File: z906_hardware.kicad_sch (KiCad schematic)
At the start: 89 parts, among them J1 USB_C_Receptacle_USB2.0_14P, J5 Ampli, J6 Console, U1 ESP32-S3-WROOM-1, U2 TPS62A02APDDC, U3 PCM5102A, U4 TPD2EUSB30, U5 TPD1E05U06DYA, U6 TPS7A4533, U7 PCM1860DBT

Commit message: correct i2s bus
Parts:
- removed C36, C38: 1nF, Capacitor_SMD:C_0603_1608Metric_Pad1.08x0.95mm_HandSolder, symbol Device:C
- removed R12, R9: 100, Resistor_SMD:R_0805_2012Metric_Pad1.20x1.40mm_HandSolder, symbol Device:R
- removed U5: TPD1E05U06DYA, Diode_SMD:D_SOD-523, symbol Power_Protection:TPD1E05U06DYA
- added D1: PESD5V0S1BL-QYL, Diode_SMD:D_SOD-882, symbol Diode:PESD5V0L1UL
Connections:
- net GND: now also D1.1 (K)
- net at U7.3 (VINL1/VIN1P): now also C35.2
- net at U7.4 (VINR1/VIN2P): now also C37.2
- net at C6.1, F1.2, FB1.1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: now also D1.2 (A)
- net ADC_DATA renamed I2S.ADC
- net BCK renamed I2S.BCK
- net DAC_DATA renamed I2S.DAC
- net LCK renamed I2S.LCK
- net MCLK renamed I2S.MCLK
- no-connect marks 27 -> 29
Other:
- moved on the sheet: C12, C13, C35, C37, C39, R10, R11, R14, R15, R22, R23, R27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

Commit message: correct usb tvs
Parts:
- removed D1: PESD5V0S1BL-QYL, Diode_SMD:D_SOD-882, symbol Diode:PESD5V0L1UL
- added D1: PESD5V0S1UB, symbol Device:D_TVS
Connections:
- net GND: now also D1.1 (A1)
- net at C6.1, F1.2, FB1.1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: now also D1.2 (A2)
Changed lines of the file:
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@@
 	)
 	(symbol
-		(lib_id "Diode:PESD5V0L1UL")
-		(at 63.5 31.75 90)
-		(unit 1)
-		(body_style 1)
-		(exclude_from_sim no)
-		(in_bom yes)
-		(on_board yes)
-		(in_pos_files yes)
-		(dnp no)
-		(fields_autoplaced yes)
-		(property "Reference" "D1"
-			(at 66.04 30.4799 90)
-			(show_name no)
-			(do_not_autoplace no)
-			(effects
-				(font
-					(size 1.27 1.27)
-				)
-				(justify right)
-			)
-		)
-		(property "Value" "PESD5V0S1BL-QYL"
-			(at 66.04 33.0199 90)
-			(show_name no)
-			(do_not_autoplace no)
-			(effects
-				(font
-					(size 1.27 1.27)
-				)
-				(justify right)
-			)
-		)
-		(property "Footprint" "Diode_SMD:D_SOD-882"
-			(at 68.58 31.75 0)
-			(hide yes)
-			(show_name no)
-			(do_not_autoplace no)
-			(effects
-				(font
-					(size 1.27 1.27)
-				)
-			)
-		)
-		(property "Datasheet" "https://assets.nexperia.com/documents/data-sheet/PESD5V0L1UL.pdf"
-			(at 58.42 31.75 0)
-			(hide yes)
-			(show_name no)
-			(do_not_autoplace no)
-			(effects
-				(font
-					(size 1.27 1.27)
-				)
-			)
-		)
-		(property "Description" "Low capacitance unidirectional ESD protection diode, 5V, SOD-882"
-			(at 55.88 31.75 0)
-			(hide yes)
-			(show_name no)
-			(do_not_autoplace no)
-			(effects
-				(font
-					(size 1.27 1.27)
-				)
-			)
-		)
-		(pin "1"
-		)
-		(pin "2"
-		)
-		(instances
-			(project "z906_hardware"
-				(path "/eb724320-f684-4550-84c5-ad44b13c3624"
-					(reference "D1")
-					(unit 1)
-				)
-			)
-		)
-	)
-	(symbol
 		(lib_id "Device:C")
 		(at 168.91 167.64 0)
@@
 					(unit 1)
 				)
+			)
+		)
+	)
+	(symbol
+		(lib_id "Device:D_TVS")
+		(at 63.5 31.75 90)
+		(unit 1)
+		(body_style 1)
+		(exclude_from_sim no)
+		(in_bom yes)
+		(on_board yes)
+		(in_pos_files yes)
+		(dnp no)
+		(fields_autoplaced yes)
+		(property "Reference" "D1"
+			(at 66.04 30.4799 90)
+			(show_name no)
+			(do_not_autoplace no)
+			(effects
+				(font
+					(size 1.27 1.27)
+				)
+				(justify right)
+			)
+		)
+		(property "Value" "PESD5V0S1UB"
+			(at 66.04 33.0199 90)
+			(show_name no)
+			(do_not_autoplace no)
+			(effects
+				(font
+					(size 1.27 1.27)
+				)
+				(justify right)
+			)
+		)
+		(property "Footprint" ""
+			(at 63.5 31.75 0)
+			(hide yes)
+			(show_name no)
+			(do_not_autoplace no)
+			(effects
+				(font
+					(size 1.27 1.27)
+				)
+			)
+		)
+		(property "Datasheet" ""
+			(at 63.5 31.75 0)
+			(hide yes)
+			(show_name no)
+			(do_not_autoplace no)
+			(effects
+				(font
+					(size 1.27 1.27)
+				)
+			)
+		)
+		(property "Description" "Bidirectional transient-voltage-suppression diode"
+			(at 63.5 31.75 0)
+			(hide yes)
+			(show_name no)
+			(do_not_autoplace no)
+			(effects
+				(font
+					(size 1.27 1.27)
+				)
+			)
+		)
+		(pin "2"
+		)
+		(pin "1"
+		)
+		(instances
+			(project "z906_hardware"
+				(path "/eb724320-f684-4550-84c5-ad44b13c3624"
+					(reference "D1")
+					(unit 1)
+				)

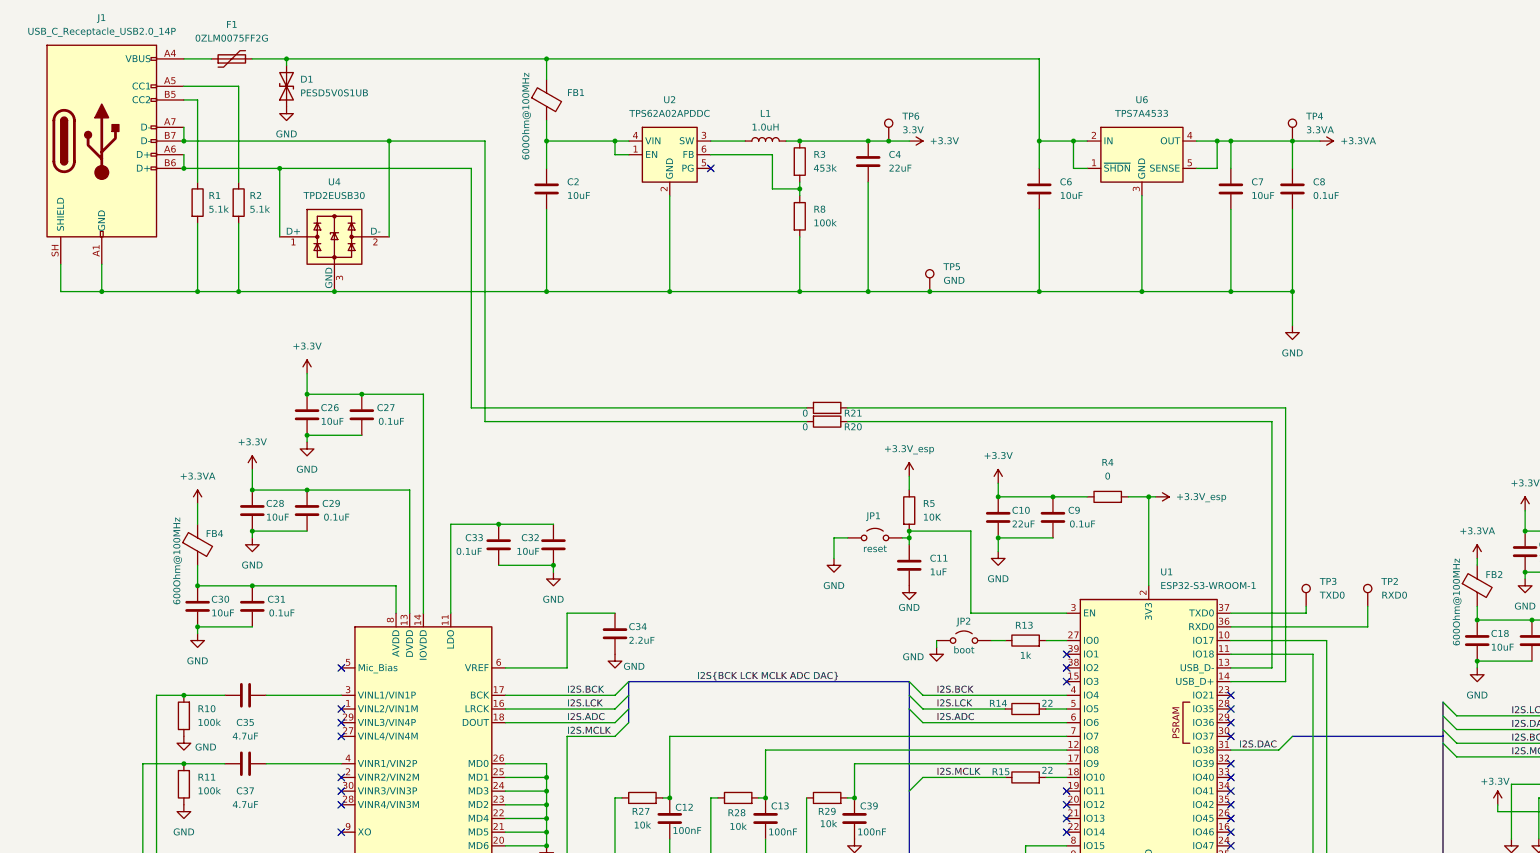
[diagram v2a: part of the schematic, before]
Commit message: change usb-c symbole for 16pin
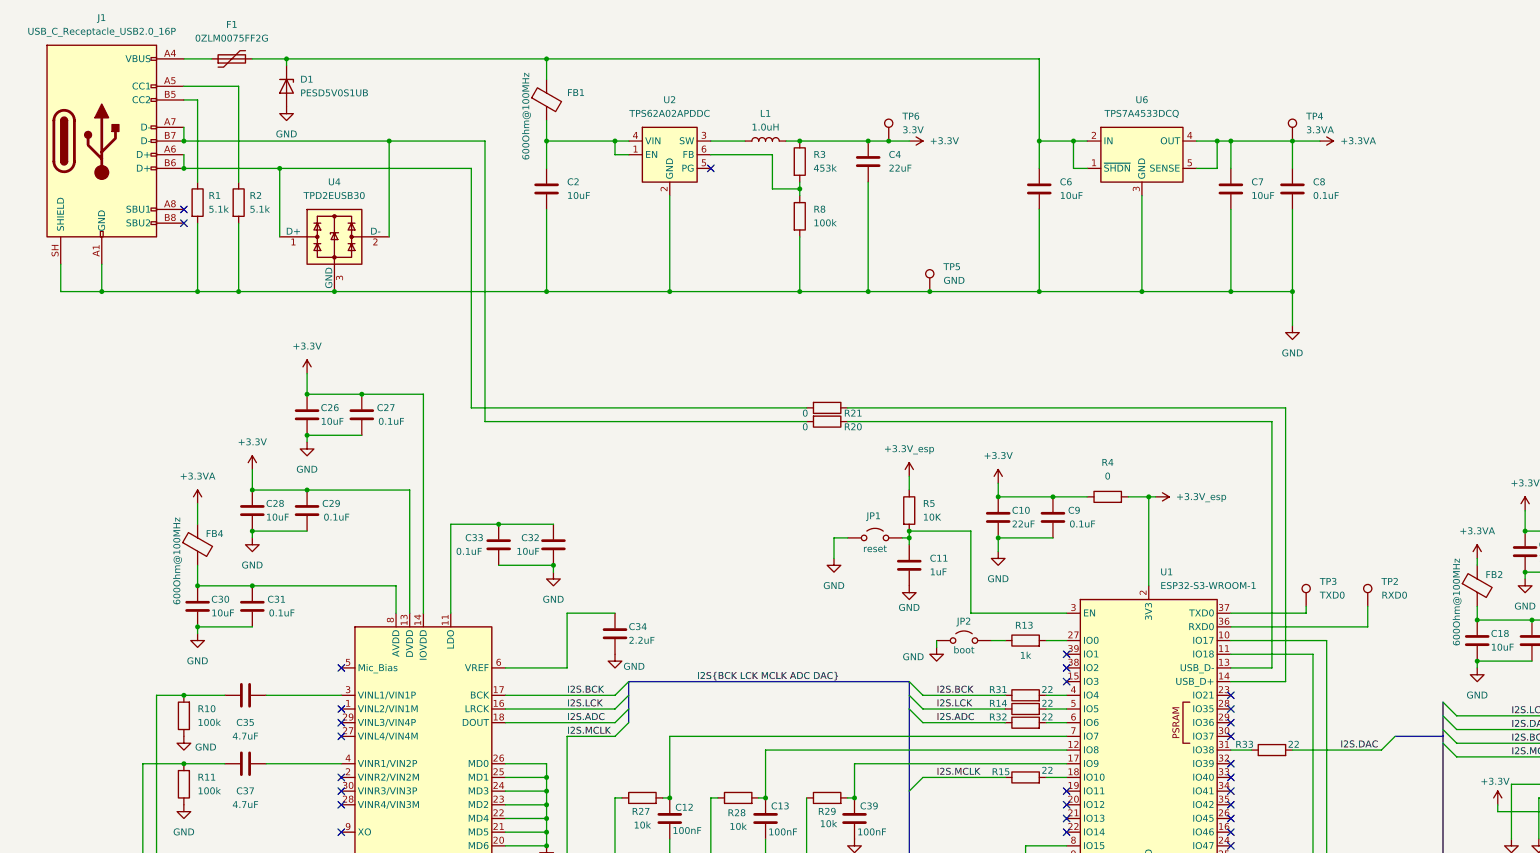
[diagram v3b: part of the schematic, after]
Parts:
- removed D1: PESD5V0S1UB, symbol Device:D_TVS
- removed J1: USB_C_Receptacle_USB2.0_14P, Connector_USB:USB_C_Receptacle_GCT_USB4105-xx-A_16P_TopMnt_Horizontal, symbol Connector:USB_C_Receptacle_USB2.0_14P
- added D1: PESD5V0S1UB, Diode_SMD:D_SOD-882, symbol Diode:PESD5V0S1UL
- added J1: USB_C_Receptacle_USB2.0_16P, symbol Connector:USB_C_Receptacle_USB2.0_16P
- added R31, R32, R33: 22, Resistor_SMD:R_0805_2012Metric_Pad1.20x1.40mm_HandSolder, symbol Device:R
- U6: value TPS7A4533 -> TPS7A4533DCQ
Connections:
- net GND: now also D1.2 (A), J1.A1 (GND), J1.A12 (GND), J1.B1 (GND), J1.B12 (GND), J1.SH (SHIELD)
- net I2S.ADC: now also R32.1; no longer U1.6 (IO6)
- net I2S.BCK: now also R31.1; no longer U1.4 (IO4)
- net I2S.DAC: now also R33.2; no longer U1.31 (IO38)
- net at R2.1: now also J1.A5 (CC1)
- net at R20.2, U4.2 (D-): now also J1.A7 (D-), J1.B7 (D-)
- net at R1.1: now also J1.B5 (CC2)
- net at F1.1: now also J1.A4 (VBUS), J1.A9 (VBUS), J1.B4 (VBUS), J1.B9 (VBUS)
- net at C6.1, F1.2, FB1.1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: now also D1.1 (K)
- net at R21.2, U4.1 (D+): now also J1.A6 (D+), J1.B6 (D+)
- new net: R31.2, U1.4 (IO4)
- new net: R33.1, U1.31 (IO38)
- new net: R32.2, U1.6 (IO6)
- no-connect marks 29 -> 31

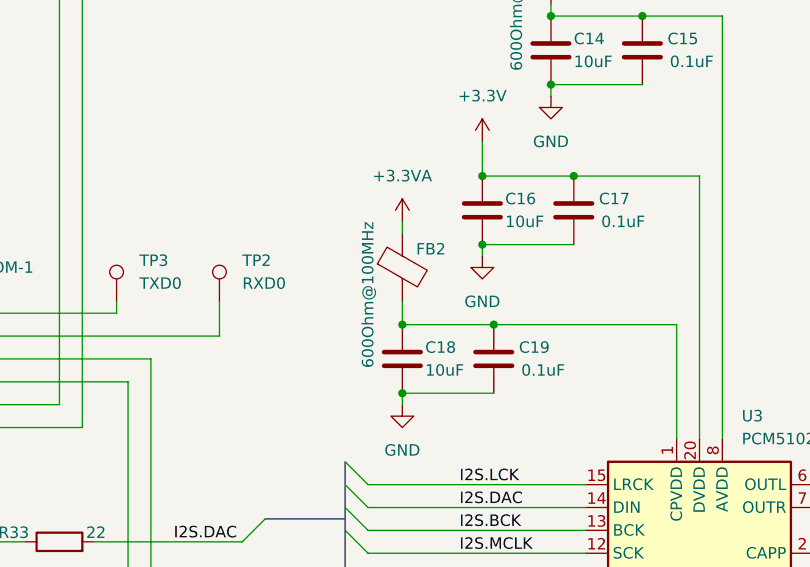
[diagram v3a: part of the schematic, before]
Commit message: remove dac fb
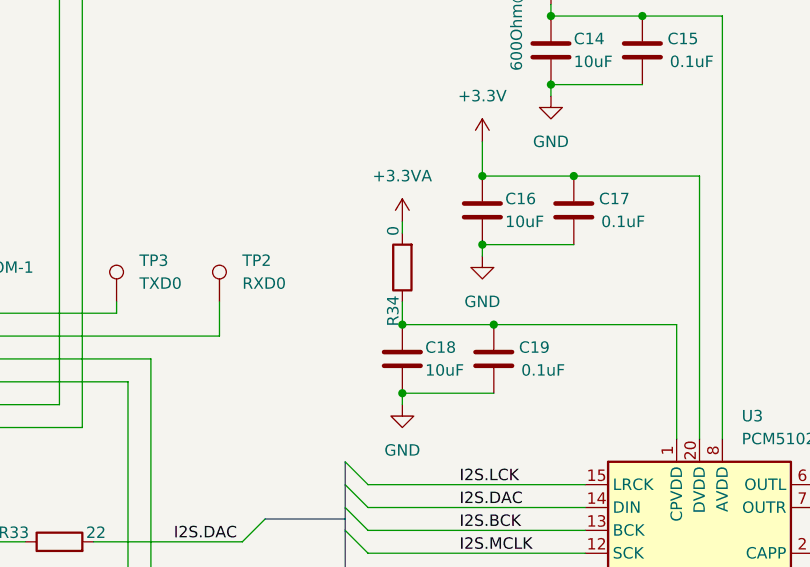
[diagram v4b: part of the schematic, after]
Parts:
- removed FB2: 600Ohm@100MHz, Resistor_SMD:R_0805_2012Metric_Pad1.20x1.40mm_HandSolder, symbol Device:FerriteBead
- added R34: 0, Resistor_SMD:R_0805_2012Metric_Pad1.20x1.40mm_HandSolder, symbol Device:R
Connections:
- net +3.3VA: now also R34.2
- net at C18.1, C19.1, U3.1 (CPVDD): now also R34.1
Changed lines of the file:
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@@
-	)
-	(symbol
-		(lib_id "Device:FerriteBead")
-		(at 284.48 124.46 0)
-		(unit 1)
-		(body_style 1)
-		(exclude_from_sim no)
-		(in_bom yes)
-		(on_board yes)
-		(in_pos_files yes)
-		(dnp no)
-		(property "Reference" "FB2"
-			(at 286.004 122.428 0)
-			(show_name no)
-			(do_not_autoplace no)
-			(effects
-				(font
-					(size 1.27 1.27)
-				)
-				(justify left)
-			)
-		)
-		(property "Value" "600Ohm@100MHz"
-			(at 280.67 135.636 90)
-			(show_name no)
-			(do_not_autoplace no)
-			(effects
-				(font
-					(size 1.27 1.27)
-				)
-				(justify left)
-			)
-		)
-		(property "Footprint" "Resistor_SMD:R_0805_2012Metric_Pad1.20x1.40mm_HandSolder"
-			(at 282.702 124.46 90)
-			(hide yes)
-			(show_name no)
-			(do_not_autoplace no)
-			(effects
-				(font
-					(size 1.27 1.27)
-				)
-			)
-		)
-		(property "Datasheet" ""
-			(at 284.48 124.46 0)
-			(hide yes)
-			(show_name no)
-			(do_not_autoplace no)
-			(effects
-				(font
-					(size 1.27 1.27)
-				)
-			)
-		)
-		(property "Description" "BLM21SP601SN1D"
-			(at 284.48 124.46 0)
-			(hide yes)
-			(show_name no)
-			(do_not_autoplace no)
-			(effects
-				(font
-					(size 1.27 1.27)
-				)
-			)
-		)
-		(pin "1"
-		)
-		(pin "2"
-		)
-		(instances
-			(project "z906_hardware"
-				(path "/eb724320-f684-4550-84c5-ad44b13c3624"
-					(reference "FB2")
-					(unit 1)
-				)
-			)
-		)
 	)
 	(symbol
@@
 					(unit 1)
 				)
+			)
+		)
+	)
+	(symbol
+		(lib_id "Device:R")
+		(at 284.48 124.46 180)
+		(unit 1)
+		(body_style 1)
+		(exclude_from_sim no)
+		(in_bom yes)
+		(on_board yes)
+		(in_pos_files yes)
+		(dnp no)
+		(property "Reference" "R34"
+			(at 283.464 129.286 90)
+			(show_name no)
+			(do_not_autoplace no)
+			(effects
+				(font
+					(size 1.27 1.27)
+				)
+			)
+		)
+		(property "Value" "0"
+			(at 283.464 120.396 90)
+			(show_name no)
+			(do_not_autoplace no)
+			(effects
+				(font
+					(size 1.27 1.27)
+				)
+			)
+		)
+		(property "Footprint" "Resistor_SMD:R_0805_2012Metric_Pad1.20x1.40mm_HandSolder"
+			(at 286.258 124.46 90)
+			(hide yes)
+			(show_name no)
+			(do_not_autoplace no)
+			(effects
+				(font
+					(size 1.27 1.27)
+				)
+			)
+		)
+		(property "Datasheet" ""
+			(at 284.48 124.46 0)
+			(hide yes)
+			(show_name no)
+			(do_not_autoplace no)
+			(effects
+				(font
+					(size 1.27 1.27)
+				)
+			)
+		)
+		(property "Description" "Resistor"
+			(at 284.48 124.46 0)
+			(hide yes)
+			(show_name no)
+			(do_not_autoplace no)
+			(effects
+				(font
+					(size 1.27 1.27)
+				)
+			)
+		)
+		(pin "1"
+		)
+		(pin "2"
+		)
+		(instances
+			(project "z906_hardware"
+				(path "/eb724320-f684-4550-84c5-ad44b13c3624"
+					(reference "R34")
+					(unit 1)
+				)

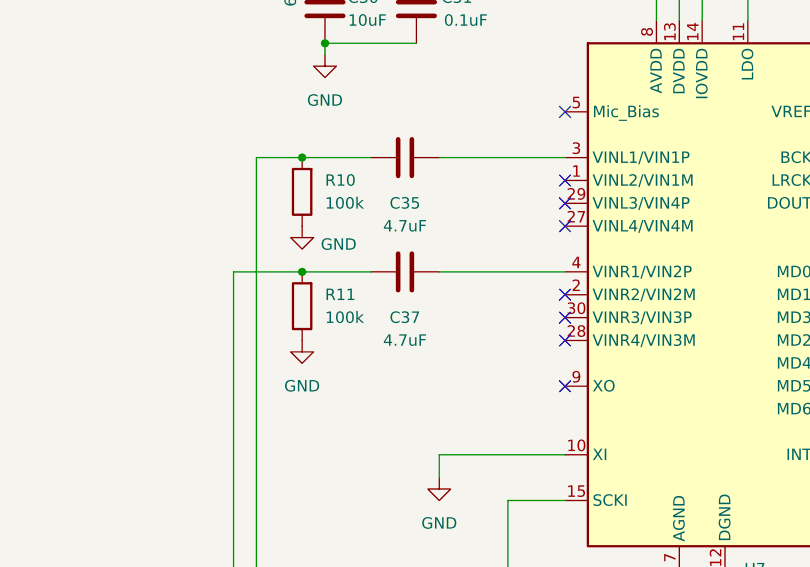
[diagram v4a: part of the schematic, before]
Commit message: use 10uF C for adc audio input
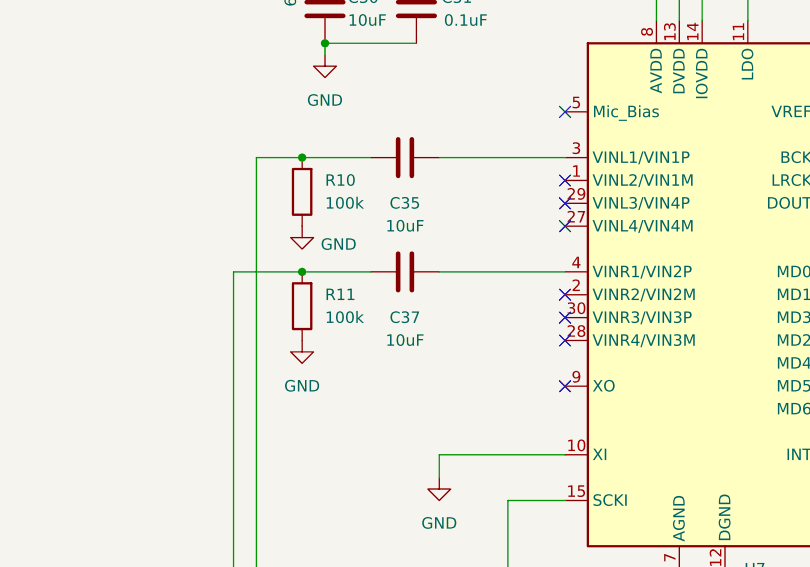
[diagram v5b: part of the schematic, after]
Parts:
- C35, C37: value 4.7uF -> 10uF
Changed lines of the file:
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@@
 			)
 		)
-		(property "Value" "4.7uF"
+		(property "Value" "10uF"
 			(at 55.88 165.1 90)
 			(show_name no)
@@
 			)
 		)
-		(property "Value" "4.7uF"
+		(property "Value" "10uF"
 			(at 55.88 152.4 90)
 			(show_name no)

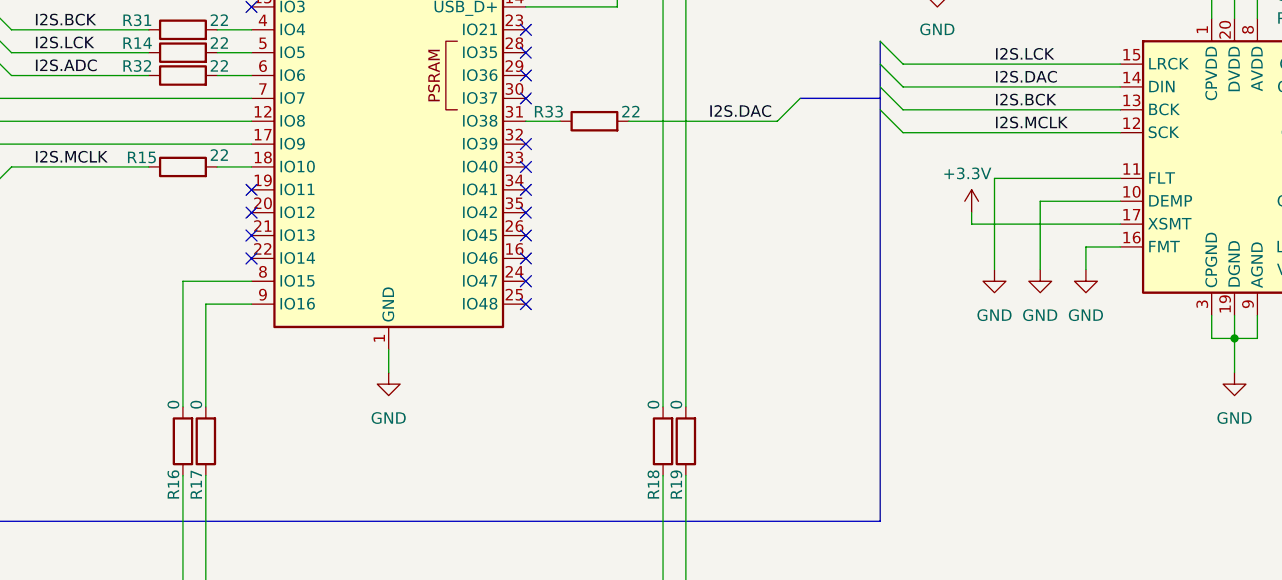
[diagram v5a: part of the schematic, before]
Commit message: use 1k ohm for uart line
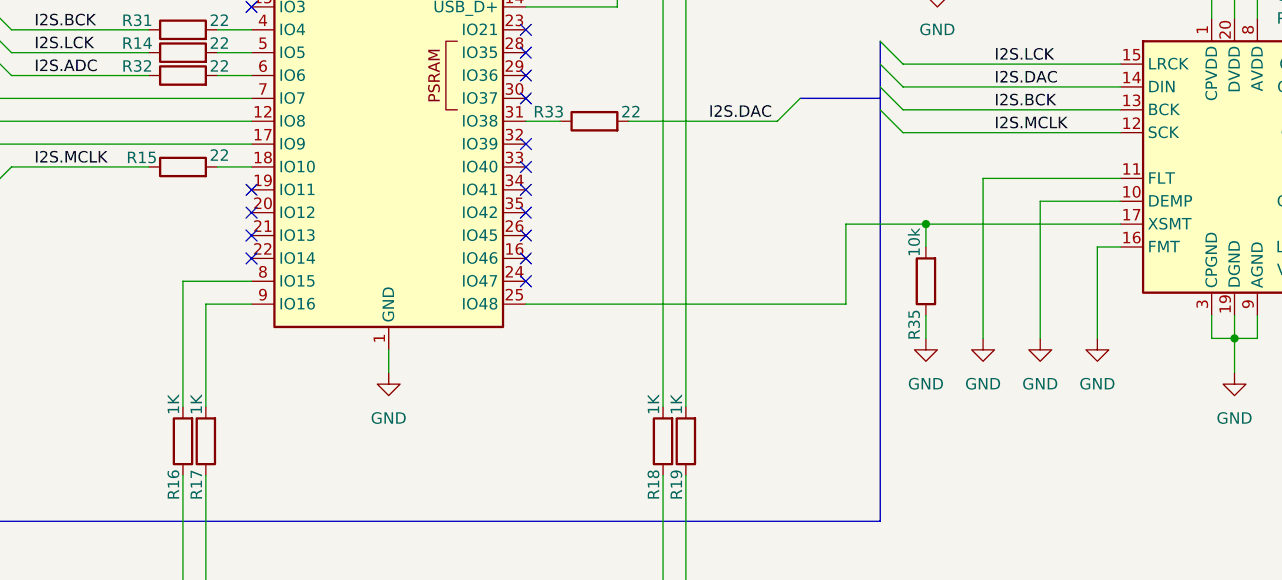
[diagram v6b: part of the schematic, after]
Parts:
- added R35: 10k, Resistor_SMD:R_0805_2012Metric_Pad1.20x1.40mm_HandSolder, symbol Device:R
- D1: footprint Diode_SMD:D_SOD-882 -> Diode_SMD:D_SOD-523
- J1: footprint (none) -> Connector_USB:USB_C_Receptacle_HCTL_HC-TYPE-C-16P-01A
- R16, R17, R18, R19: value 0 -> 1K
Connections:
- net +3.3V: no longer U3.17 (XSMT)
- net GND: now also R35.1
- net at U1.25 (IO48): now also U3.17 (XSMT), R35.2
- no-connect marks 31 -> 30
